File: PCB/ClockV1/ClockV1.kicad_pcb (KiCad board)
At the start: 2 copper layers, 50 x 30 mm, 45 parts, among them J1 Conn_01x02, J2 Conn_01x02, J3 Conn_01x08, J4 Conn_01x02, Q1 FDN327N, Q2 DMP2045UQ-7, U1 MT3608, U2 MAX14611ETD_, U3 DFR0299, U4 ATtiny1616-M

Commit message: Production to JLCPCB
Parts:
- added H5: MountingHole, MountingHole:ToolingHole_1.152mm, F.Cu at (29.5, 39.0)
- added H6: MountingHole, MountingHole:ToolingHole_1.152mm, F.Cu at (73.0, 44.5)
- added H7: MountingHole, MountingHole:ToolingHole_1.152mm, F.Cu at (56.0, 63.5)
- D2: value BAT43 -> LBAT46T1G
- D3: value LED -> Red
- D4: value LED -> Green
- Q2: value DMP2045UQ-7 -> AO3407A; footprint Samacsys:SOT96P240X110-3N -> Package_TO_SOT_SMD:SOT-23-3
- R2: value 442k -> 330k
- U2: value MAX14611ETD_ -> MAX14611ETD+T
- moved C1 1.00 mm to (27.1, 43.0)
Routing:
- net LDR_EN: track 33.3 -> 32.4 mm
- net +3V0: track 27.2 -> 26.6 mm
- net GND: vias 46 -> 47

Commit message: Add decoupling capacitors and signal selection jumper for MAX14611
- Added decoupling capacitors (C5/100nF and C6/1uF) for the MAX14611 dual power supplies
- Added solder jumper to allow selection between PON and BR signals for microcontroller input
- Renamed net HBR to Net-(JP2-C) to better reflect its function as jumper connection
- Added new HPONBR signal net for level shifter power control
- Updated PCB date to 2025-05-11
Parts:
- added C5: 100nF, Capacitor_SMD:C_0603_1608Metric, F.Cu at (49.8, 40.8)
- added C6: 1uF, Capacitor_SMD:C_0603_1608Metric, F.Cu at (49.0, 43.2)
- added JP2: PON/BR Select, Jumper:SolderJumper-3_P1.3mm_Open_RoundedPad1.0x1.5mm, B.Cu at (42.0, 41.2)
- added kibuzzard-681FCE61: G***, kibuzzard-681FCE61, B.Cu at (42.0, 43.8)
- added kibuzzard-681FCEAB: G***, kibuzzard-681FCEAB, B.Cu at (49.8, 42.8)
- JP1: moved to B.Cu
- TP2: value HBR -> HPONBR
- moved JP1 1.35 mm to (52.5, 41.5)
- moved kibuzzard-681BEBFE 0.38 mm to (38.0, 42.1)
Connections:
- net HBR renamed HPONBR
- U2 pad 2: BR -> Net-(JP2-C)
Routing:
- net PON: track 8.04 -> 17.7 mm
- net Net-(JP2-C): track 0.00 -> 7.75 mm, vias 0 -> 1
- net BR: track 3.89 -> 9.52 mm
- net Net-(JP1-C): track 13.4 -> 8.27 mm, vias 0 -> 1
- net +3V3: track 46.5 -> 51.0 mm
- net RF: track 17.8 -> 14.3 mm
- net GND: track 13.3 -> 16.0 mm, vias 47 -> 46
- net +1V5: track 18.5 -> 17.7 mm, vias 1 -> 2

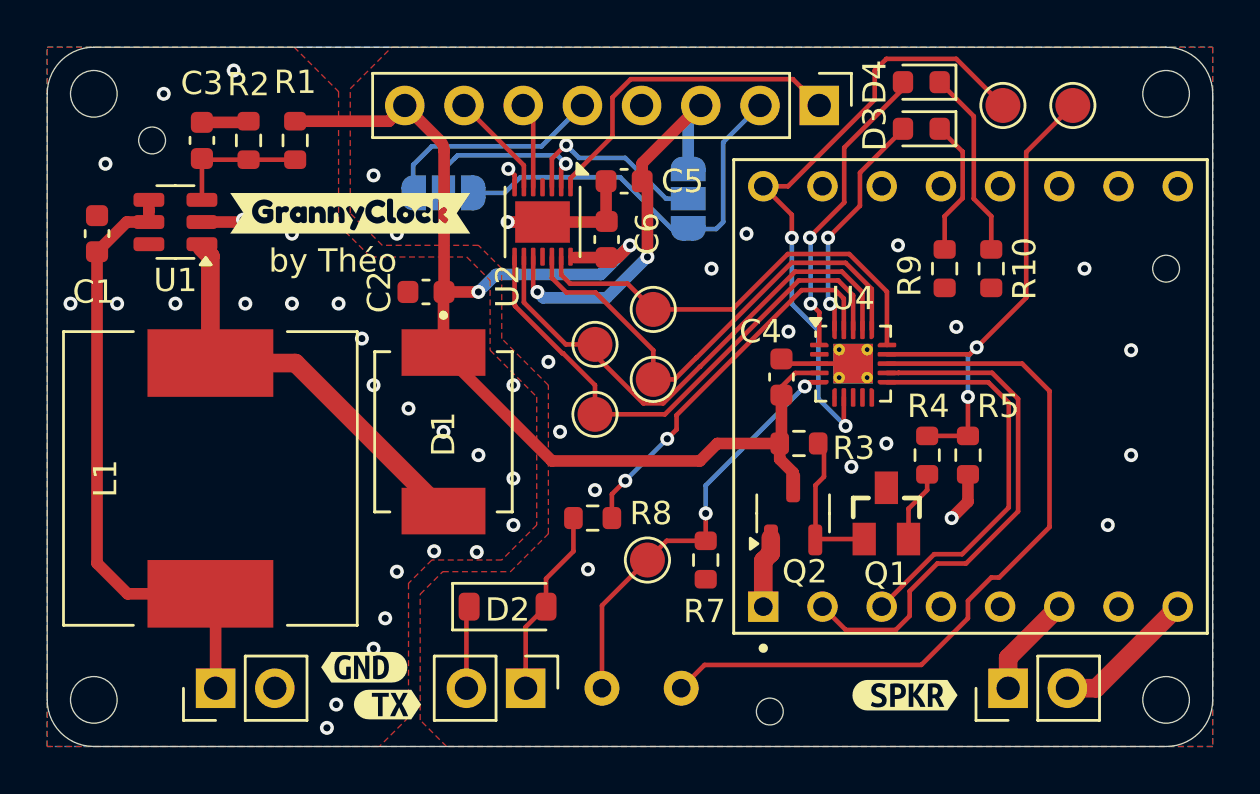
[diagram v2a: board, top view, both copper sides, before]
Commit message: Update of PCB ClockV1
- Export Silkscreen in 3D
- Add jumper to select monitoring PON
- Re-order references
- Monitor +3V0 from uC with ADC and a decoupling capactior
- Changed photoresistor footprint (actual part is smaller than expected)
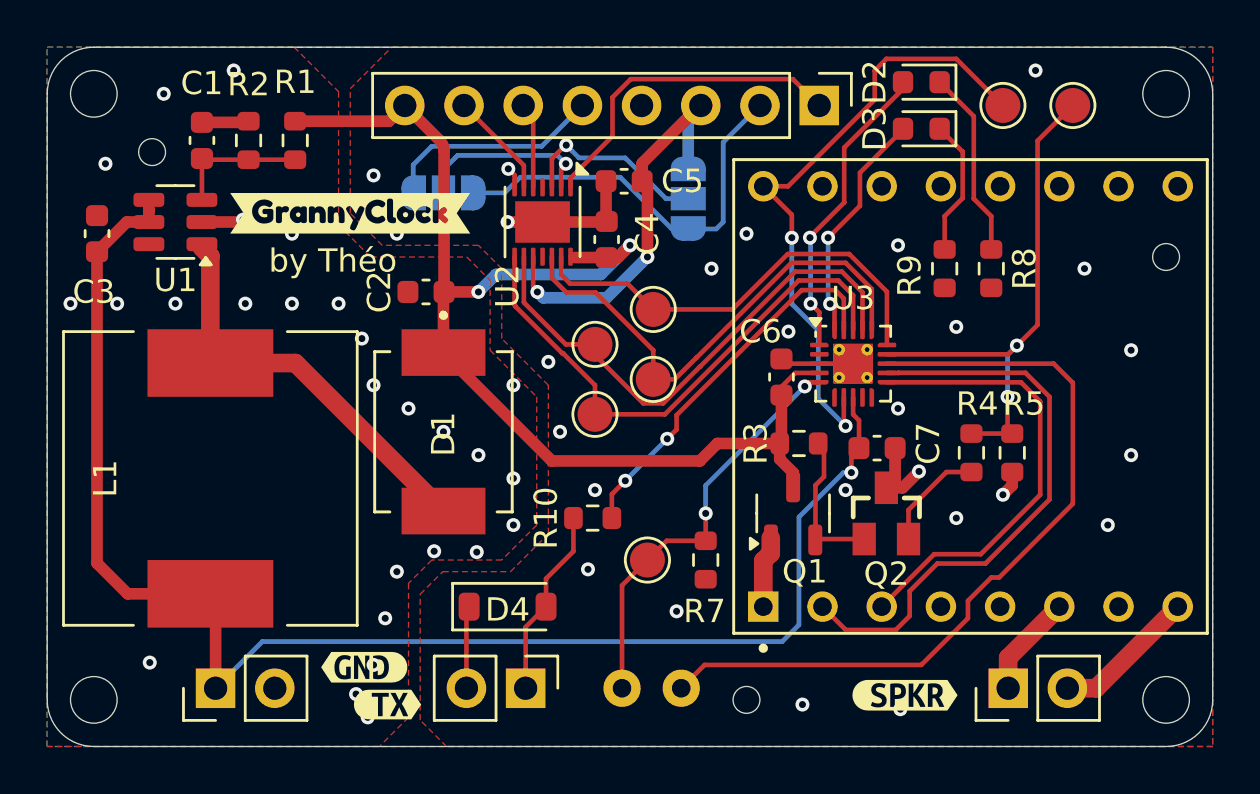
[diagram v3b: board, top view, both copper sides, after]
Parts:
- added C7: 100nF, Capacitor_SMD:C_0603_1608Metric, F.Cu at (60.6, 52.2)
- H5, H6, H7: value MountingHole -> ToolingHole
- R6: footprint OptoDevice:R_LDR_5.1x4.3mm_P3.4mm_Vertical -> OptoDevice:R_LDR_4.9x4.2mm_P2.54mm_Vertical
- moved R4 1.90 mm to (64.7, 52.4)
- moved R5 1.90 mm to (66.4, 52.4)
- moved H7 1.12 mm to (55.0, 63.0)
- moved H5 0.50 mm to (29.5, 39.5)
- moved H6 0.50 mm to (73.0, 44.0)
- renumbered C3 to C1, C1 to C3, C6 to C4, C4 to C6, D4 to D2, D2 to D4, Q2 to Q1, Q1 to Q2, R8 to R10, R10 to R8, TP7 to TP1, TP1 to TP3, TP3 to TP4, TP4 to TP5, TP5 to TP7, U4 to U3, U3 to U4
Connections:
- U3 pad 8: unconnected-(U4-PA7-Pad8) -> +3V0
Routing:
- net +3V0: track 26.6 -> 63.9 mm, vias 0 -> 1
- net GND: track 16.0 -> 18.6 mm, vias 46 -> 53
- net SND_RX: track 22.5 -> 24.9 mm
- net SND_TX: track 17.3 -> 19.7 mm
- net LDR_EN: track 32.4 -> 34.0 mm
- net Net-(Q2-G): track 3.11 -> 4.62 mm
- net DFR_EN: track 21.8 -> 22.8 mm
- net LDR_MES: track 18.5 -> 17.9 mm

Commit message: Add switch to PCB
- Added a single push button switch
- Added RC filter for (pre-)debounce
- Moved tooling hole to place the button
- Removed some silkscreen labels to make room
- Renumbered components depengind on their placement on the PCB
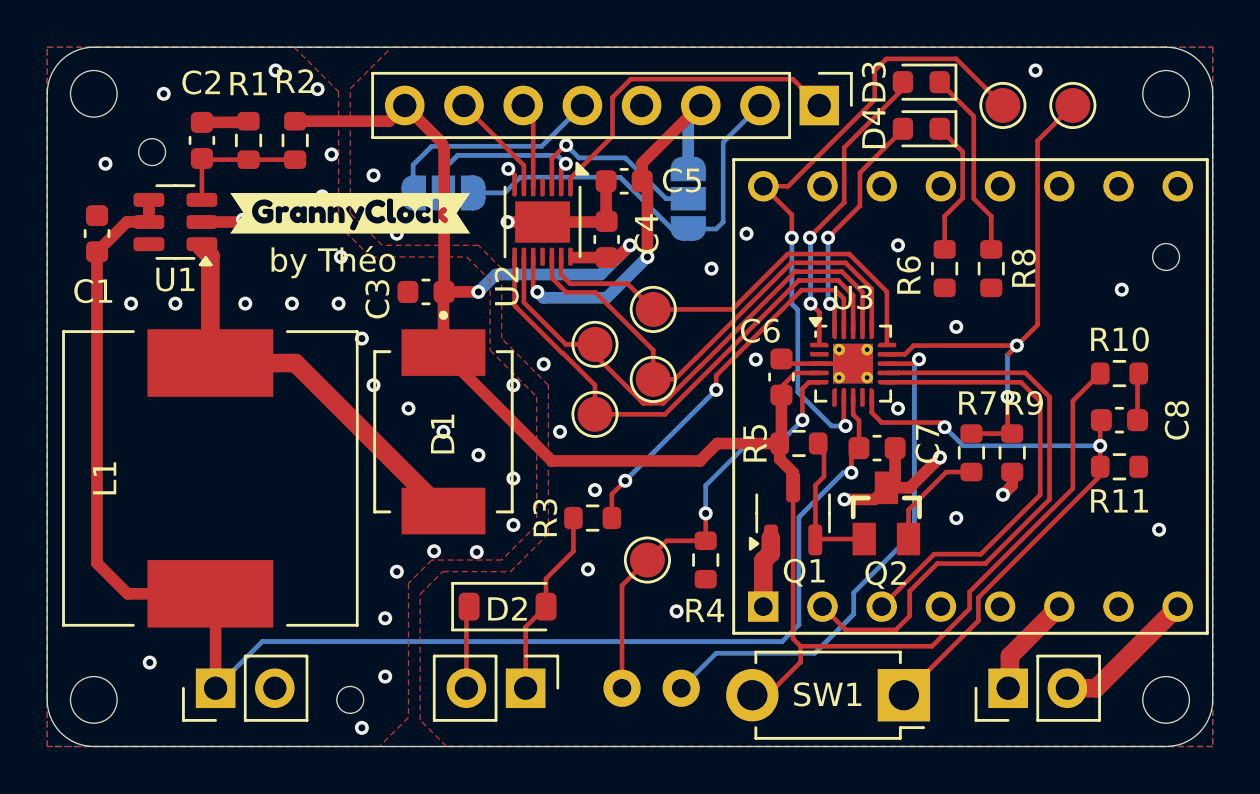
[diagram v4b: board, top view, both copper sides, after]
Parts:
- removed kibuzzard-681BEACB: G***, kibuzzard-681BEACB
- removed kibuzzard-681BEB3E: G***, kibuzzard-681BEB3E
- removed kibuzzard-681BEB6B: G***, kibuzzard-681BEB6B
- added C8: 100nF, Capacitor_SMD:C_0603_1608Metric, F.Cu at (71.0, 51.0)
- added R10: 100, Resistor_SMD:R_0603_1608Metric, F.Cu at (71.0, 49.0)
- added R11: 10k, Resistor_SMD:R_0603_1608Metric, F.Cu at (71.0, 53.0)
- added SW1: SW_Push, Button_Switch_THT:SW_PUSH_1P1T_6x3.5mm_H4.3_APEM_MJTP1243, F.Cu at (61.8, 62.8)
- moved H4 17.0 mm to (38.0, 63.0)
- renumbered C3 to C1, C1 to C2, C2 to C3, D4 to D2, D2 to D3, D3 to D4, H4 to H2, H5 to H3, H7 to H4, H2 to H5, H3 to H7, J4 to J2, J2 to J4, R2 to R1, R6 to R12, R1 to R2, R10 to R3, R7 to R4, R3 to R5, R9 to R6, R4 to R7, R5 to R9, TP4 to TP1, TP5 to TP2, TP7 to TP3, TP3 to TP4, TP2 to TP5, TP1 to TP7, kibuzzard-681BEBFE to kibuzzard-1, kibuzzard-681FCEAB to kibuzzard-2, kibuzzard-681FCE61 to kibuzzard-3
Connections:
- U3 pad 10: unconnected-(U3-PB4-Pad10) -> BTN
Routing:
- net +3V3: track 51.0 -> 81.7 mm
- net BTN: track 0.00 -> 26.4 mm, vias 0 -> 2
- net LDR_EN: track 34.0 -> 22.3 mm, vias 0 -> 1
- net GND: track 18.6 -> 21.7 mm, vias 53 -> 50
- net Net-(C8-Pad1): track 0.00 -> 2.02 mm
- net LDR_MES: track 17.9 -> 18.7 mm
- net DFR_EN: track 22.8 -> 23.3 mm

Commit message: Corrected debouncer
- Capacitor was not positionned properly
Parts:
- moved SW1 6.30 mm to (55.5, 62.7), turned to 0 degrees
- moved R11 4.10 mm to (71.0, 53.1), turned to 180 degrees
- moved R10 4.00 mm to (71.0, 49.0)
- turned C8 to 0 degrees
- renumbered R11 to R10, R10 to R11
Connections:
- C8 pad 1: Net-(C8-Pad1) -> BTN
- C8 pad 2: BTN -> GND
- R11 pad 1: +3V3 -> Net-(R11-Pad1)
- R11 pad 2: Net-(C8-Pad1) -> BTN
- SW1 pad 1: BTN -> +3V3
- SW1 pad 2: +3V3 -> Net-(R11-Pad1)
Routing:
- net +3V3: track 81.7 -> 61.2 mm
- net Net-(R11-Pad1): track 0.00 -> 15.4 mm
- net BTN: track 26.4 -> 15.3 mm
- net Net-(C8-Pad1): track 2.02 -> 0.00 mm
- net GND: track 21.7 -> 23.7 mm, vias 50 -> 53
- net DFR_EN: track 23.3 -> 22.8 mm

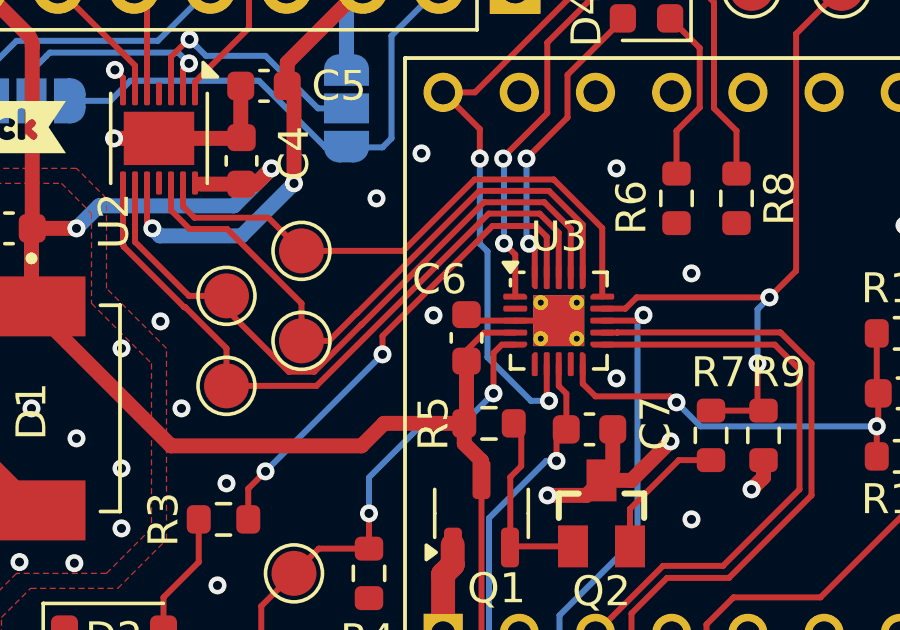
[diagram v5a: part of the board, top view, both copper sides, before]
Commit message: Store last changes in ClockV1 before deprecating
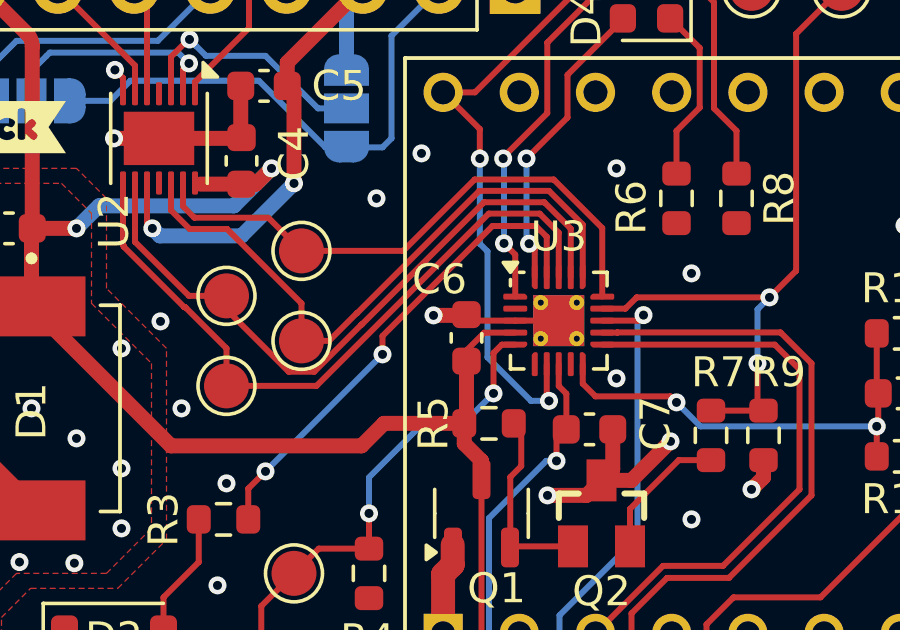
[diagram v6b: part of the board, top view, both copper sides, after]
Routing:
- net GND: track 23.7 -> 24.9 mm
